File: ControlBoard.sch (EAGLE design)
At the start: 98 parts, among them CON1 CONN_20, CON2 CONN_20, CON3 CONN_20, CON4 CONN_20, CON5 CONN_2

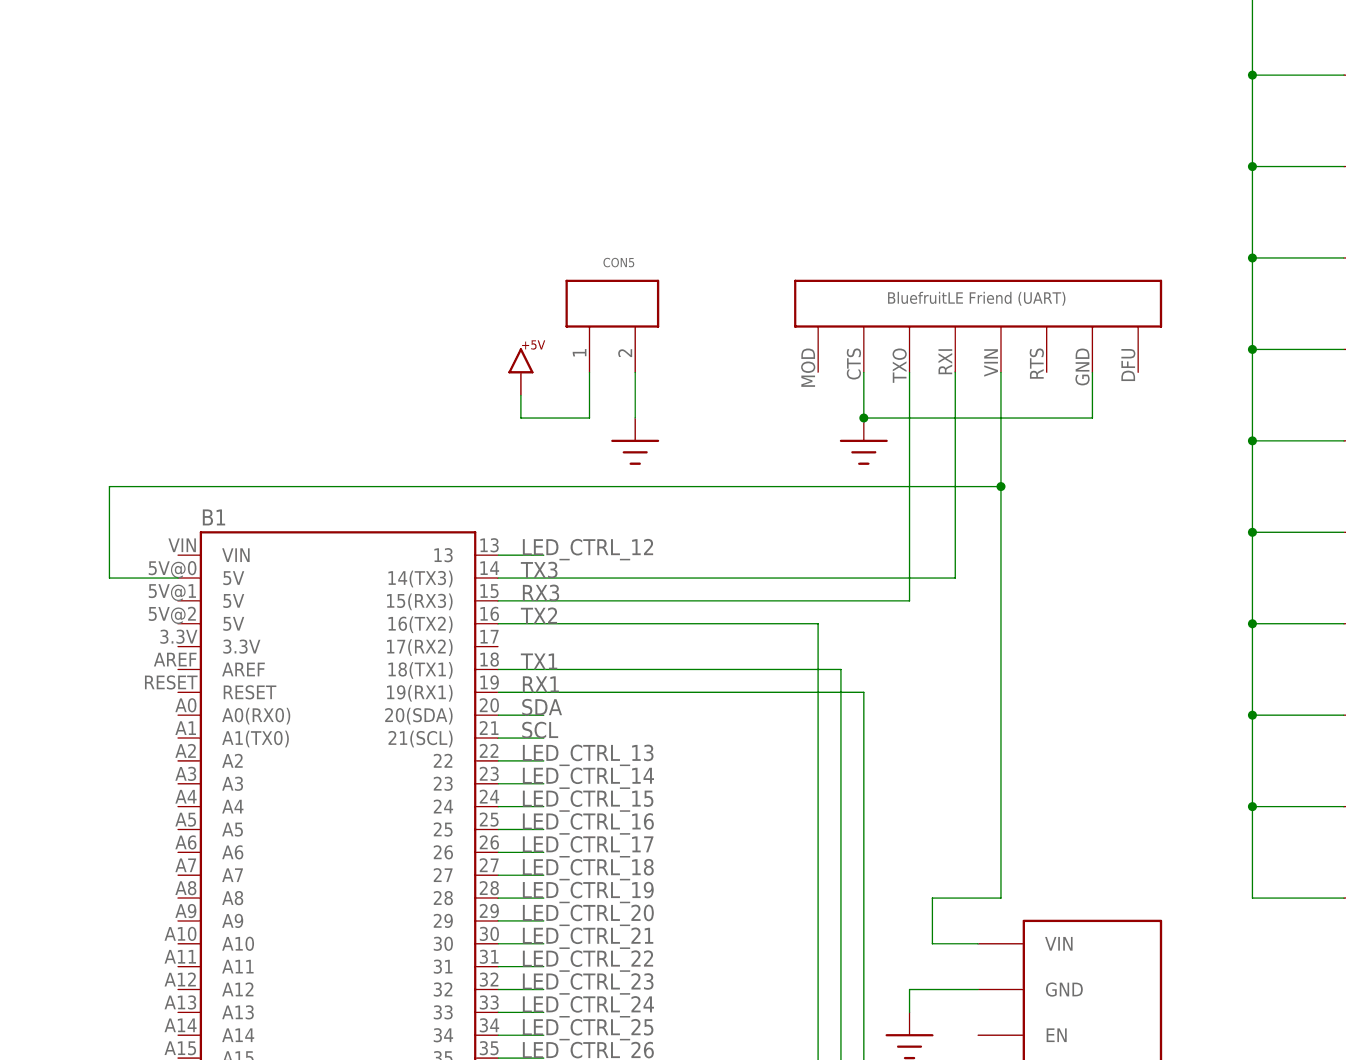
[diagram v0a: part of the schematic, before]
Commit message: Final refinements before first order
— Connected DFU and MOD pins of BLE UART board
— Tented vias
— Fixed DRC stop mask errors
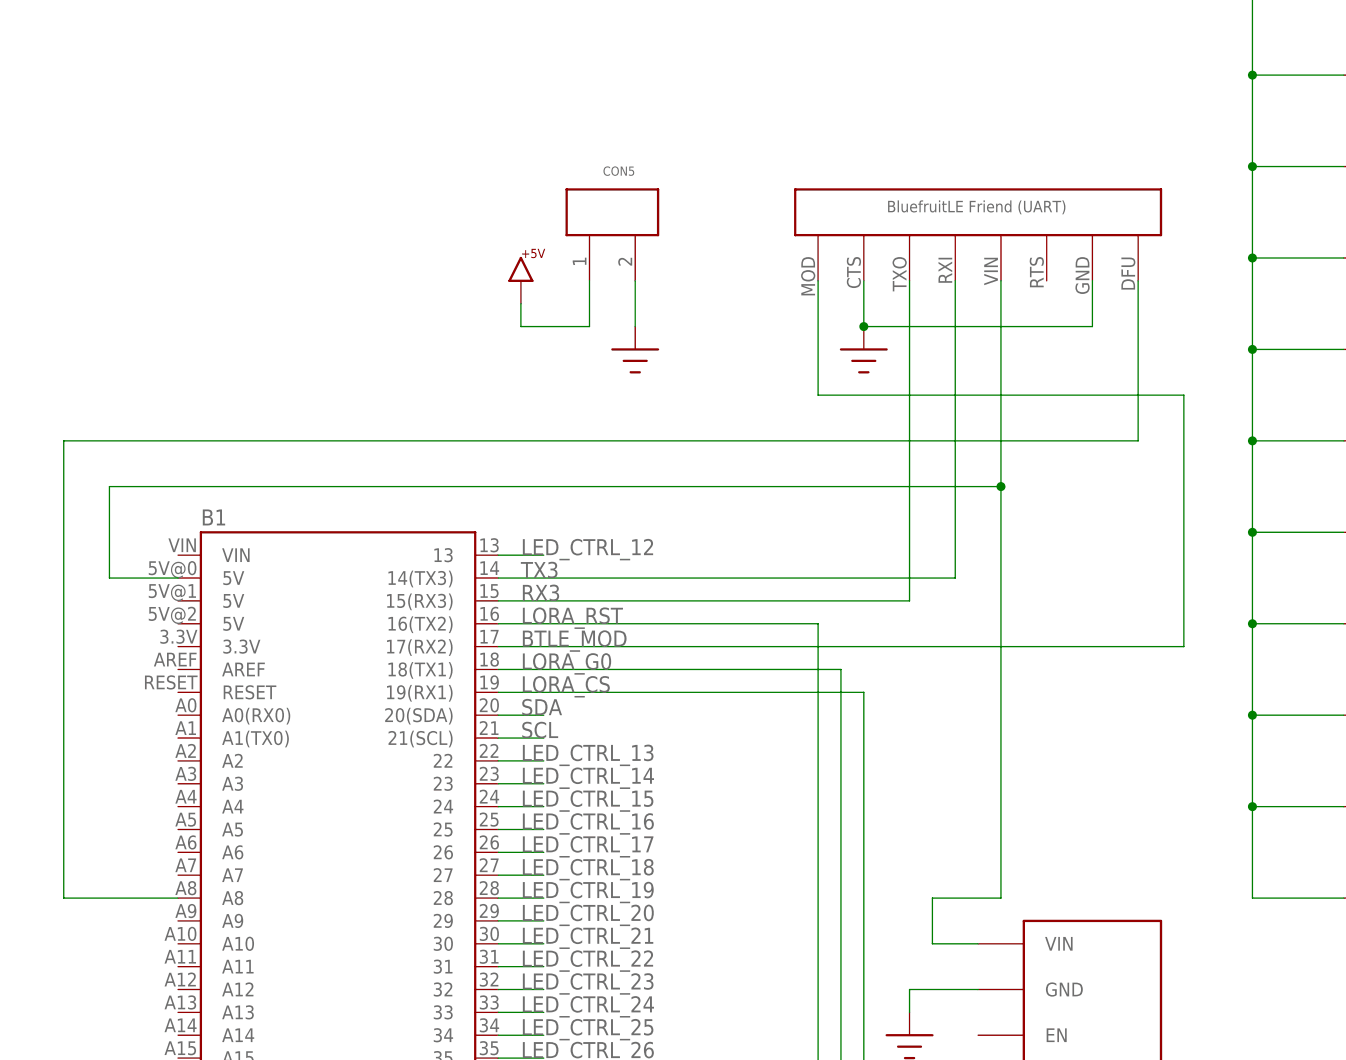
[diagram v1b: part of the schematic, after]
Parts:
- renumbered U$11 to R46, U$12 to R41, U$23 to R47, U$24 to R42, U$33 to R48, U$34 to R43, U$45 to R49, U$46 to R44, U$57 to R50, U$58 to R45
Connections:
- net RX1 renamed LORA_CS
- net TX1 renamed LORA_G0
- net TX2 renamed LORA_RST
- new net BTLE_DFU: B1.A8, U$62.P$8
- new net BTLE_MOD: B1.17(RX2), U$62.P$1
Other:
- moved on the sheet: CON5
